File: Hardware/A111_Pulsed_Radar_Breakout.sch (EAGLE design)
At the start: 26 parts, among them J4 RASPBERRYPI-26-PIN-GPIO, U1 A111, U2 1.8V, U4 TXB0108DQSR, Y1 26MHz

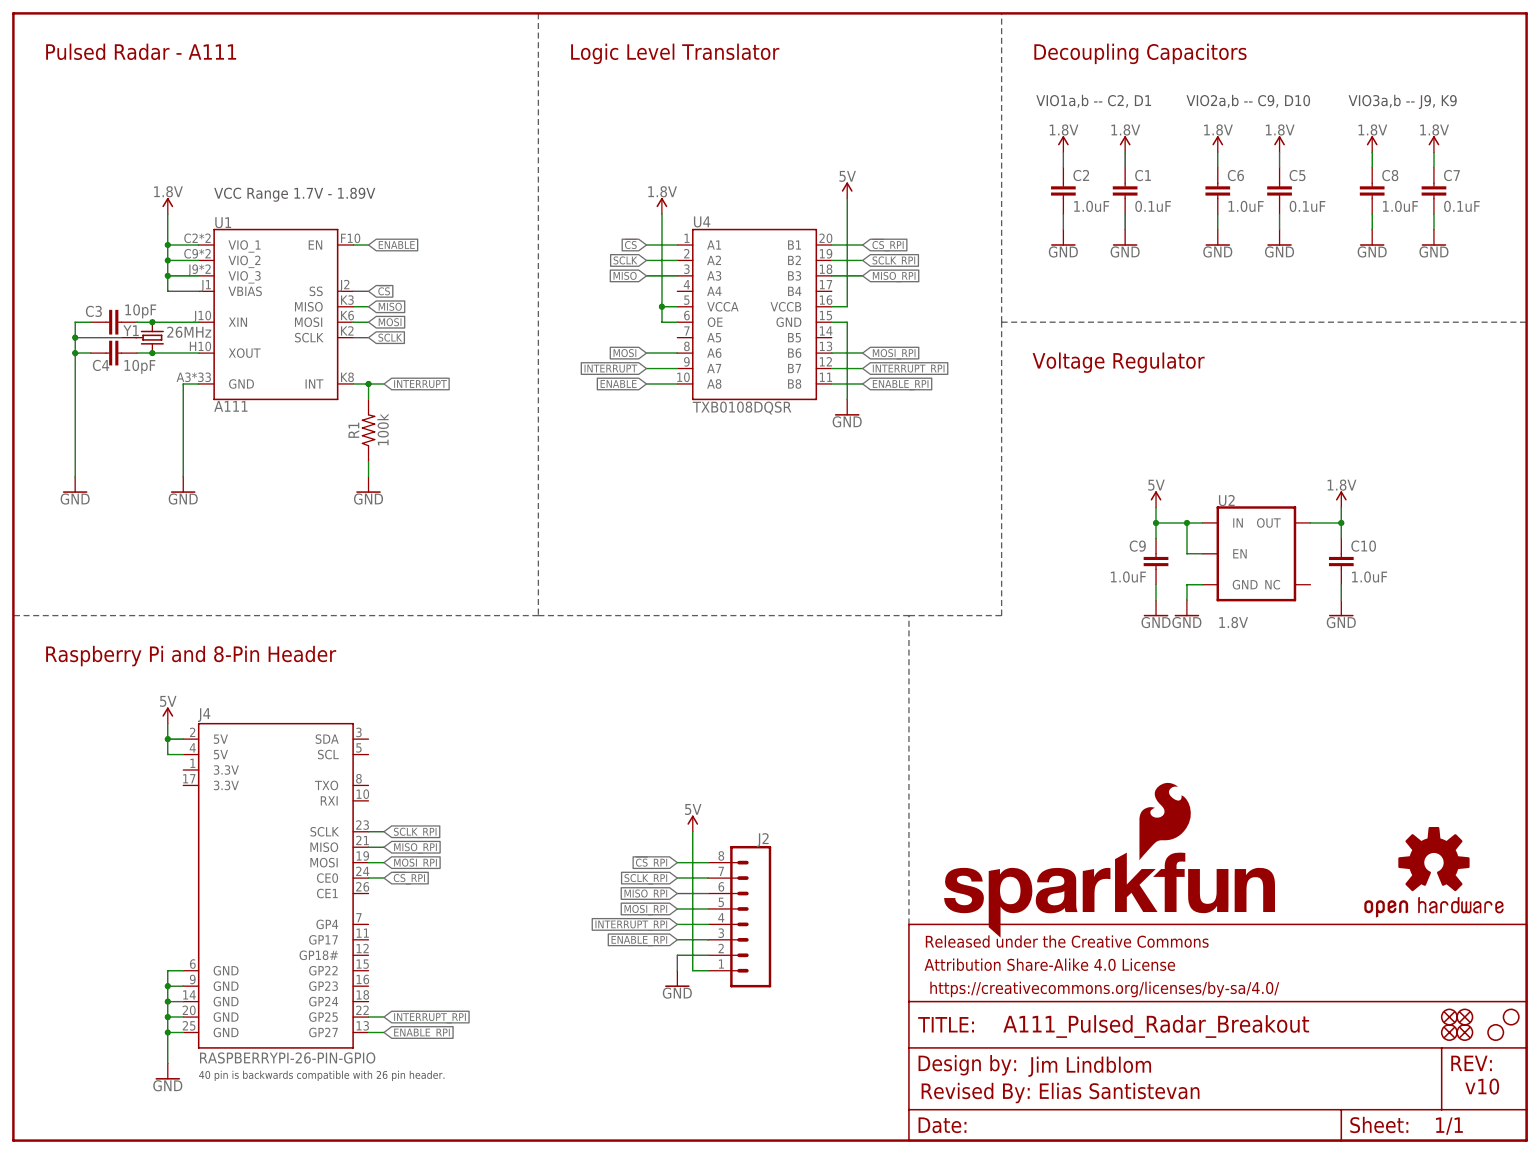
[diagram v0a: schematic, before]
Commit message: Splits power to level translation so that it's at on a separate power bus (3.3V on Rasp Pi)
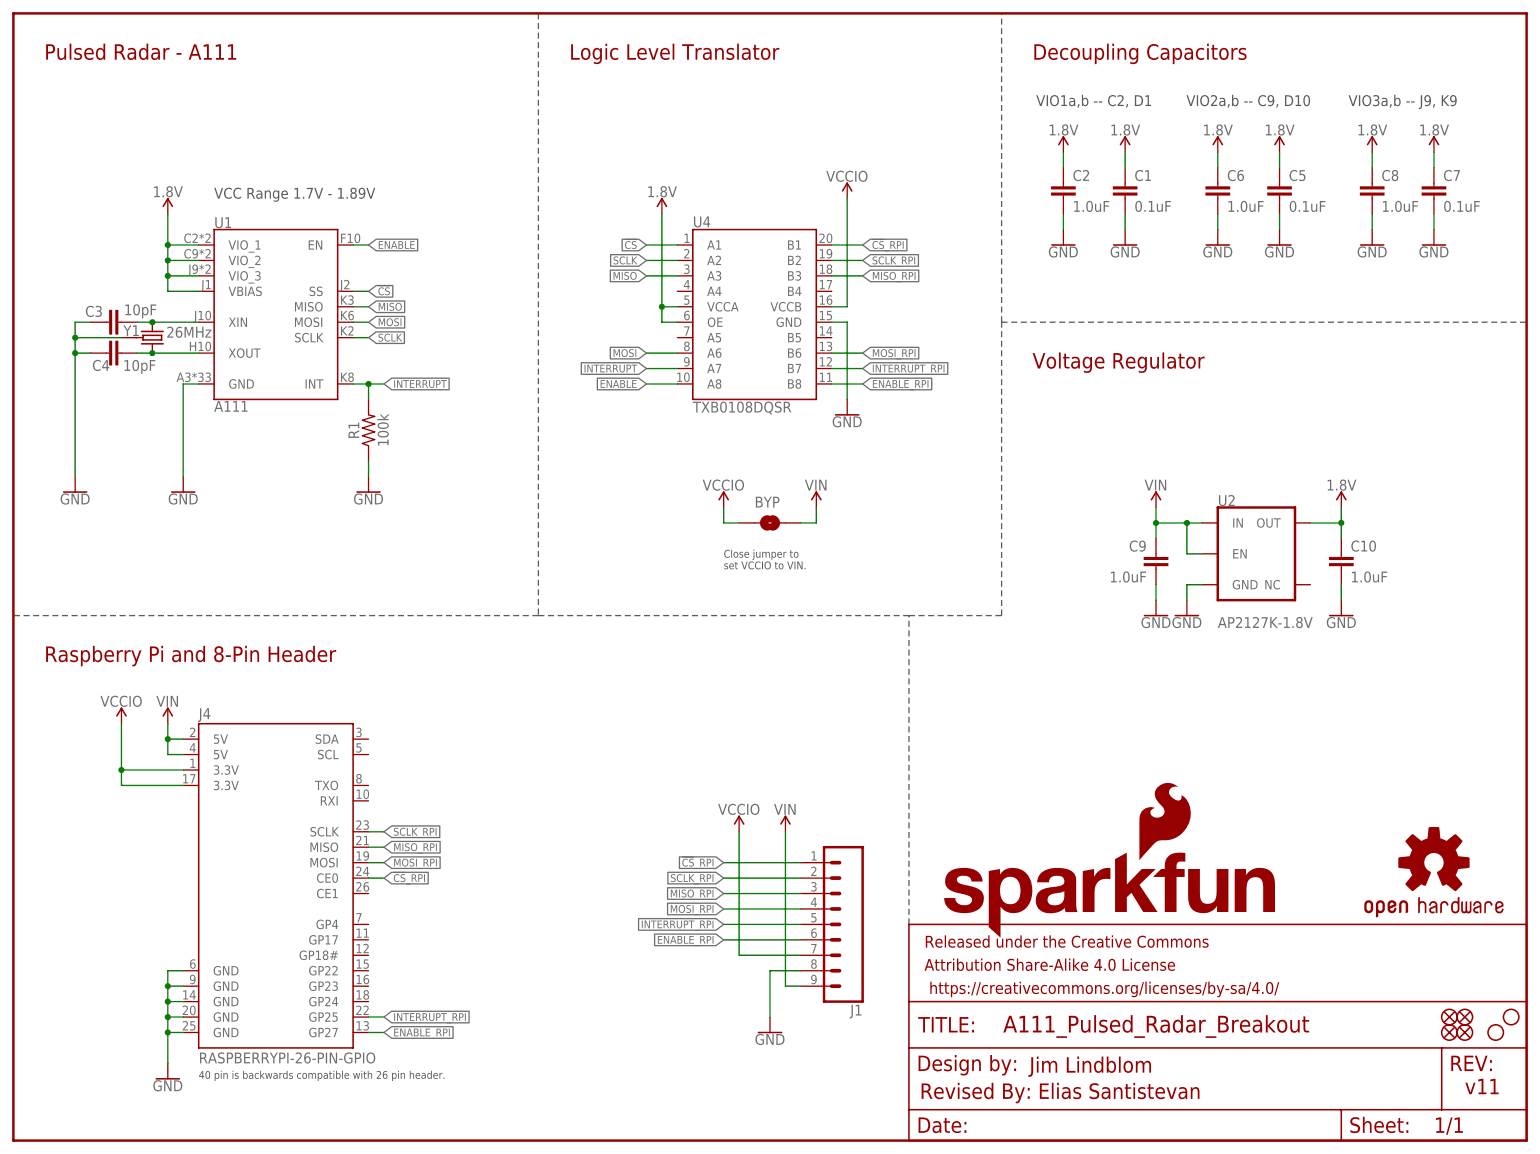
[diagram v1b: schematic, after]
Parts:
- removed J2: (no value), SparkFun-Connectors:CONN_08NO_SILK_FEMALE_PTH
- added BYP: JUMPER-SMT_2_NO_SILK, SparkFun-Jumpers:JUMPER-SMT_2_NO_SILK
- added J1: (no value), SparkFun-Connectors:CONN_09NO_SILK
- LOGO2: value OSHW-LOGOM -> OSHW-LOGOS; device SparkFun-Aesthetics:OSHW-LOGOM -> SparkFun-Aesthetics:OSHW-LOGOS
- U2: value 1.8V -> AP2127K-1.8V
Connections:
- removed net 5V: C9.1, J2.1, J4.5V@2, J4.5V@4, U2.EN, U2.IN, U4.VCCB
- new net VCCIO: BYP.1, J1.7, J4.3.3V@1, J4.3.3V@17, U4.VCCB
- new net VIN: BYP.2, C9.1, J1.9, J4.5V@2, J4.5V@4, U2.EN, U2.IN
- net !CS!_RPI: now also J1.1; no longer J2.8
- net ENABLE_RPI: now also J1.6; no longer J2.3
- net GND: now also J1.8, Y1.GND; no longer J2.2, Y1.3
- net INTERRUPT_RPI: now also J1.5; no longer J2.4
- net MISO_RPI: now also J1.3; no longer J2.6
- net MOSI_RPI: now also J1.4; no longer J2.5
- net SCLK_RPI: now also J1.2; no longer J2.7
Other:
- note added: "Close jumper to set VCCIO to VIN."
- note added: "v11"
- note removed: "v10"
